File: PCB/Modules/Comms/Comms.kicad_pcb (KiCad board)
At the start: 4 copper layers, 50 x 50 mm, 52 parts, among them J1 In, J10 1PPS In, J11 32MHz Out, J12 Shield, J13 Shield, J14 BATT +, J15 BATT -, J2 Test, J3 Bus, J4 Bus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

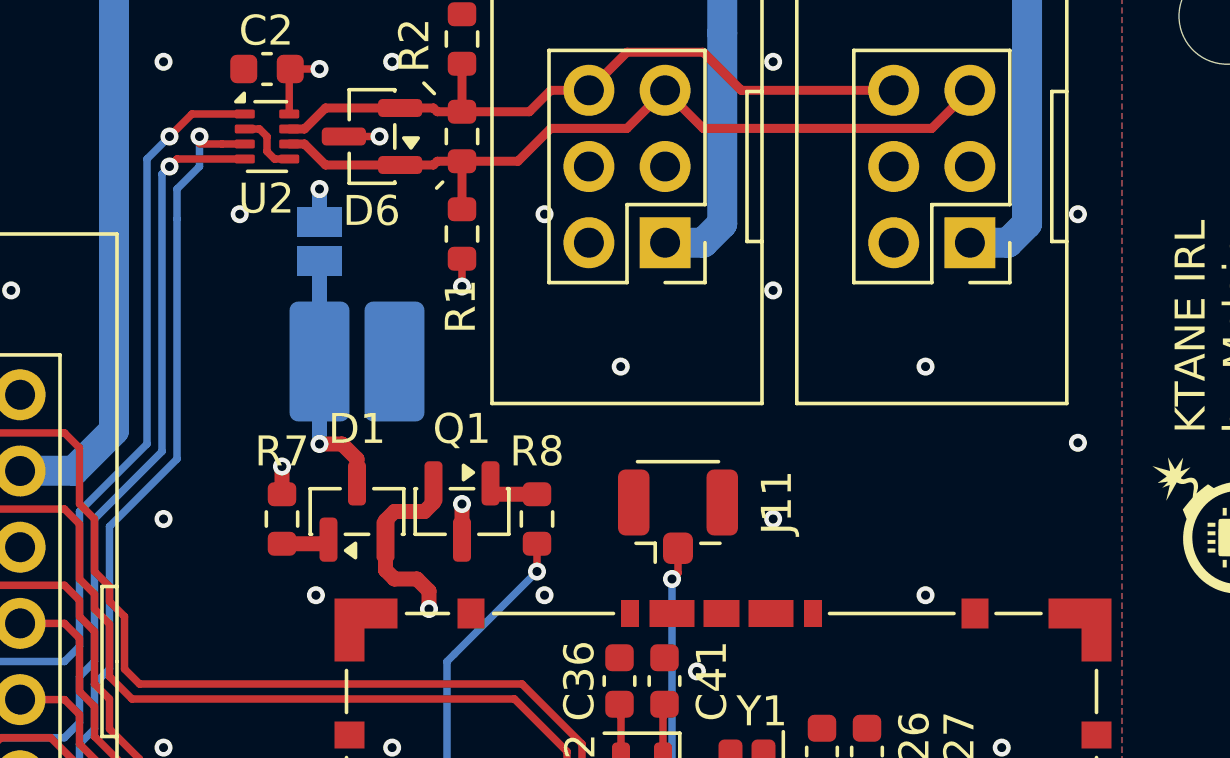
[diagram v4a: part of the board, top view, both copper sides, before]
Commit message: feat: Replace bare pads for battery with a cell, incase we want to use a cell holder.
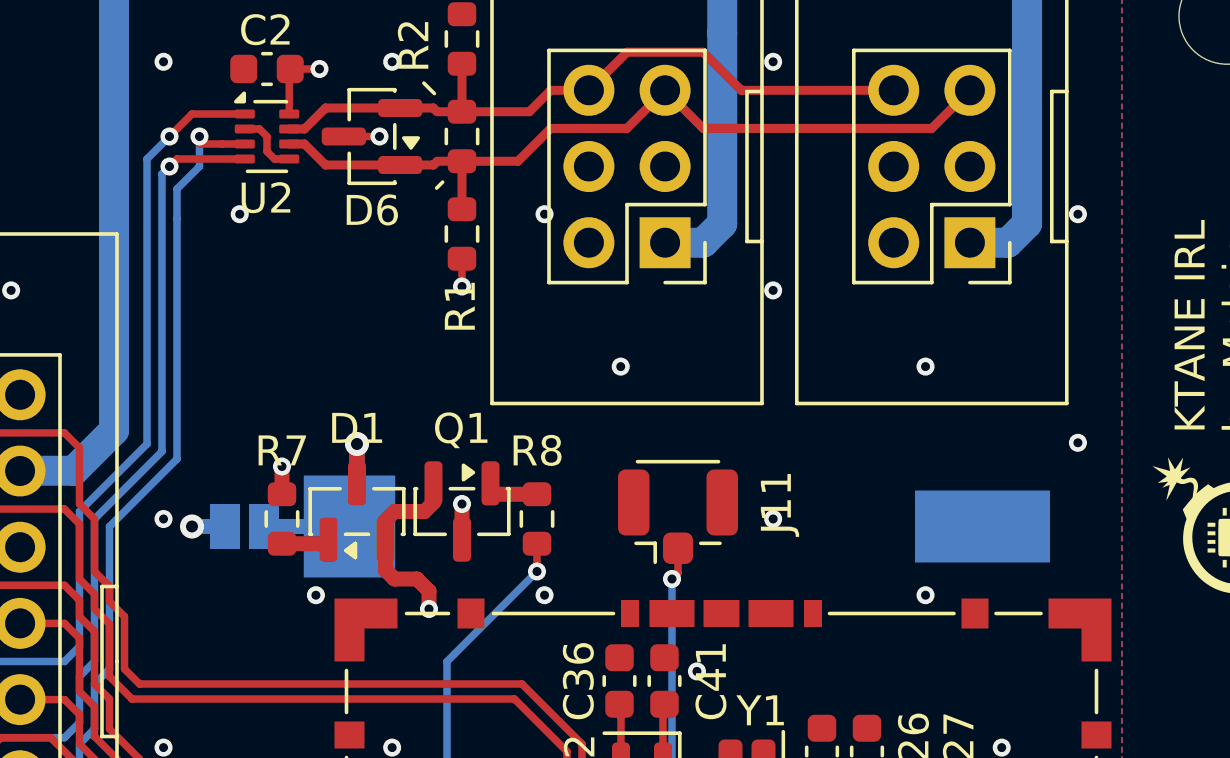
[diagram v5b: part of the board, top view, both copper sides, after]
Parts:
- removed J14: BATT +, KTANE:Pad4x2
- removed J15: BATT -, KTANE:Pad4x2
- added BT1: MR2032, KTANE:CellHolder, B.Cu at (50.9, 40.5)
- moved JP1 9.82 mm to (33.8, 40.5), turned to 0 degrees
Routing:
- net Net-(BT1-+): track 8.37 -> 7.02 mm
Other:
- board text added: "+"
- board text added: "-"
